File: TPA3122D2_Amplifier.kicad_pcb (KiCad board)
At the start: 2 copper layers, 80 x 80 mm, 51 parts, among them J1 Barrel_Jack_Switch, J2 Screw_Terminal_01x02, J3 AudioJack3, J4 Screw_Terminal_01x04, Q1 TSM480P06, SW1 SW_Push_SPDT, U1 TPA3122D2

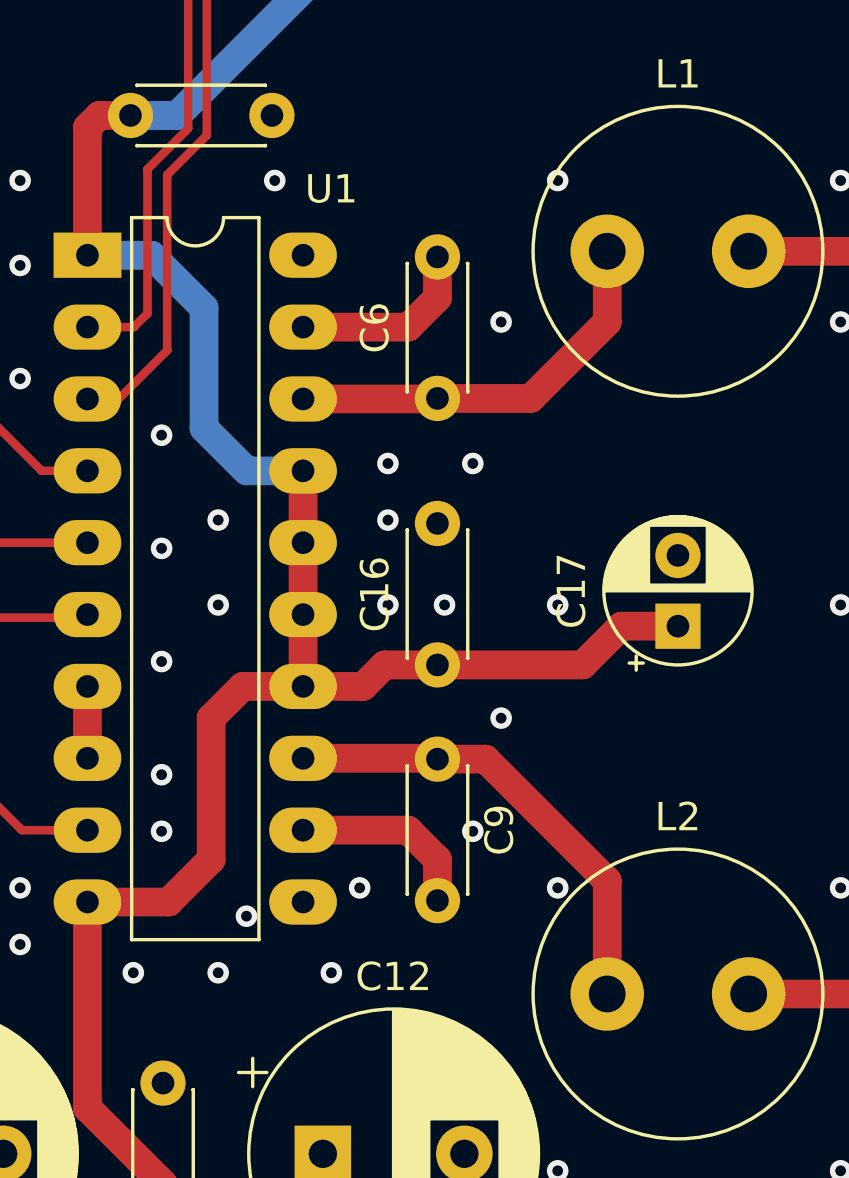
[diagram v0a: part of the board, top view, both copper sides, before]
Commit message: fixed misplaced capacitors C6 & C9
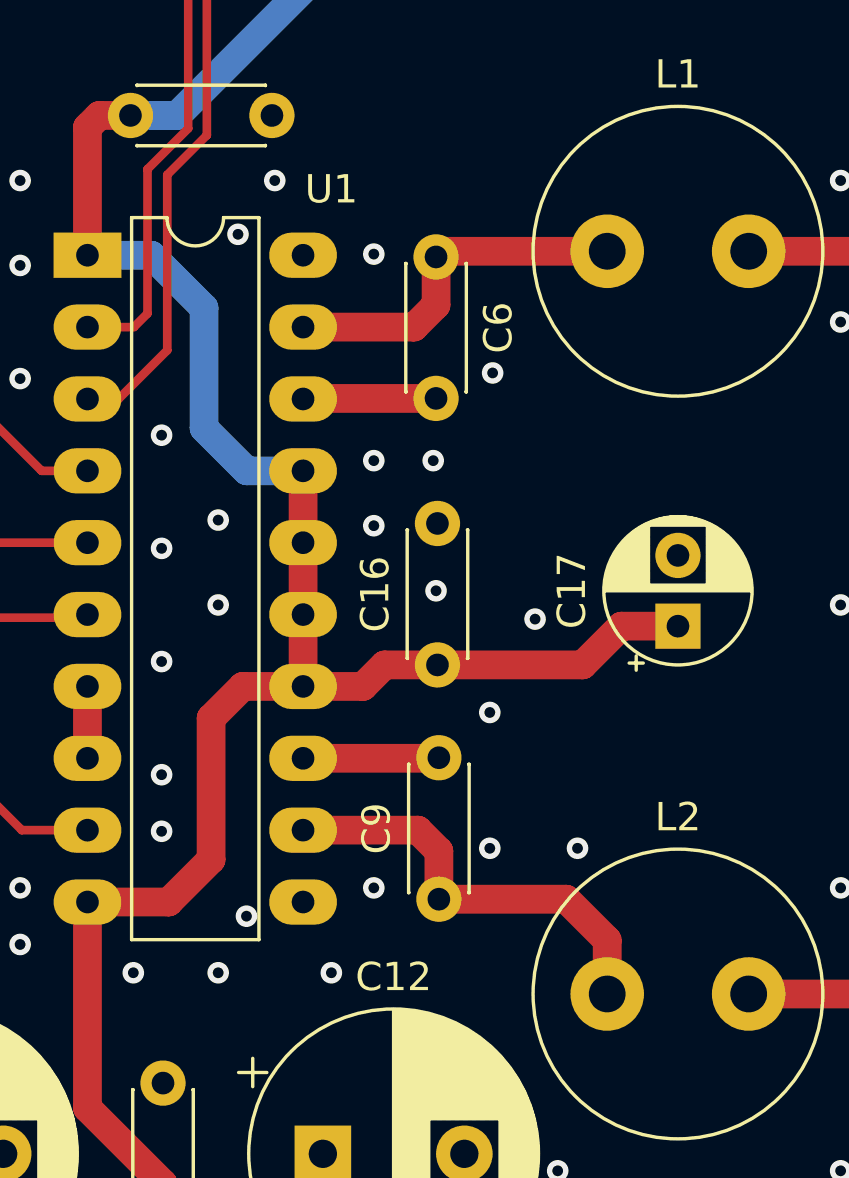
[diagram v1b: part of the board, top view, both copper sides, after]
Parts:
- moved C6 5.00 mm to (140.7, 77.7), turned to -90 degrees
- moved C9 4.95 mm to (140.8, 100.4), turned to 90 degrees
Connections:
- C6 pad 1: BSL -> LOUT
- C6 pad 2: LOUT -> BSL
- C9 pad 1: BSR -> ROUT
- C9 pad 2: ROUT -> BSR
- L1 pad 1: BSL -> LOUT
- L2 pad 1: BSR -> ROUT
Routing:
- net BSR: track 16.5 -> 4.81 mm
- net BSL: track 14.4 -> 4.71 mm
- net ROUT: track 6.63 -> 15.3 mm
- net LOUT: track 6.63 -> 12.9 mm

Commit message: updated audio connector
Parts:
- J3: footprint Connector_Audio:Jack_3.5mm_CUI_SJ1-3533NG_Horizontal -> myparts:Jack_3.5mm_CUI_SJ1-3523N_Horizontal
- moved H1 70.0 mm to (105.0, 55.0)
- moved H2 70.0 mm to (175.0, 55.0)
- moved H3 70.0 mm to (105.0, 125.0)
- moved H4 70.0 mm to (175.0, 125.0)
- moved Q1 5.62 mm to (118.2, 123.3)
- moved D1 4.20 mm to (123.0, 127.9)
- moved J2 2.10 mm to (107.0, 107.6)
- moved RV1 2.00 mm to (106.5, 80.0)
- moved SW1 2.00 mm to (106.6, 87.0)
- moved REF** 1.92 mm to (116.9, 54.7)
- moved J1 1.80 mm to (114.8, 116.3)
- moved J3 1.49 mm to (107.2, 65.0), turned to -90 degrees
- moved D2 0.40 mm to (143.4, 123.5)
- moved JP2 0.06 mm to (127.8, 59.0)
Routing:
- net Net-(J3-PadT): track 28.2 -> 12.7 mm
- net Net-(J3-PadR): track 24.3 -> 32.4 mm
- net /VIN2: track 40.0 -> 47.6 mm
- net /VIN1: track 40.8 -> 34.4 mm
- net Net-(D1-A): track 20.3 -> 15.8 mm
- net VCC: track 217.0 -> 220.3 mm
- net Net-(C18-Pad1): track 12.9 -> 10.6 mm

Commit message: fixed terminal blocks
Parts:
- J2: footprint TerminalBlock:TerminalBlock_Altech_AK300-2_P5.00mm -> TerminalBlock_Phoenix:TerminalBlock_Phoenix_MKDS-1,5-2_1x02_P5.00mm_Horizontal
- J4: footprint TerminalBlock:TerminalBlock_Altech_AK300-4_P5.00mm -> TerminalBlock_Phoenix:TerminalBlock_Phoenix_MKDS-1,5-4_1x04_P5.00mm_Horizontal
- moved J4 15.1 mm to (173.8, 97.6), turned to 90 degrees
- moved J2 5.20 mm to (106.0, 102.5), turned to -90 degrees
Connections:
- J4 pad 1: /POWC -> /POWD
- J4 pad 4: /POWD -> /POWC
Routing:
- net /VIN1: track 34.4 -> 37.7 mm
- net GND: vias 78 -> 96
